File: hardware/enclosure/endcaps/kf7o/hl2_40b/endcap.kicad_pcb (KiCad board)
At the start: 2 copper layers, 106 x 40 mm, 45 parts, among them J2 Male Header, J3 Male Header, J4 Fan, Q1 DTC144E, Q2 IRLML6402, Q3 MULTIFET, Q4 MULTIFET, Q5 MULTIFET, Q6 MULTIFET, Q7 MULTIFET, U1 ACPL-M21L-000E

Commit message: Final IO end plates
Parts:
- added G***: OSHW-logo_silkscreen-back_2mm, HERMESLITE:OSHW-logo_silkscreen-back_2mm, B.Cu at (127.1, 55.1)
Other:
- board text added: "HL2 IO End Plate v1.0 © 2019 SofterHardware"
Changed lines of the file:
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@@
   (general
     (thickness 1.6)
-    (drawings 24)
+    (drawings 25)
     (tracks 281)
     (zones 0)
-    (modules 45)
+    (modules 46)
     (nets 29)
   )
@@
   (title_block
     (title "Hermes-Lite End Plate 40")
-    (date 2019-11-24)
+    (date 2019-12-01)
     (rev 2.0)
     (company SofterHardware)
@@
     )
   )
+  (module HERMESLITE:OSHW-logo_silkscreen-back_2mm (layer B.Cu)
+    (at 127.1 55.1 180)
+    (fp_text reference G*** (at 0 -1.05918 180) (layer B.SilkS) hide
+      (effects (font (size 0.0889 0.0889) (thickness 0.01778)) (justify mirror))
+    )
+    (fp_text value OSHW-logo_silkscreen-back_2mm (at 0 1.05918 180) (layer B.SilkS) hide
+      (effects (font (size 0.0889 0.0889) (thickness 0.01778)) (justify mirror))
+    )
+    (fp_poly (pts (xy 0.60452 -0.89662) (xy 0.59436 -0.89154) (xy 0.5715 -0.8763) (xy 0.53848 -0.85598)
+      (xy 0.49784 -0.82804) (xy 0.45974 -0.80264) (xy 0.42672 -0.77978) (xy 0.40386 -0.76454)
+      (xy 0.3937 -0.75946) (xy 0.38862 -0.762) (xy 0.37084 -0.77216) (xy 0.3429 -0.78486)
+      (xy 0.32766 -0.79248) (xy 0.30226 -0.80518) (xy 0.28956 -0.80772) (xy 0.28702 -0.80264)
+      (xy 0.27686 -0.78486) (xy 0.26416 -0.75184) (xy 0.24384 -0.70866) (xy 0.22352 -0.65786)
+      (xy 0.20066 -0.60198) (xy 0.1778 -0.5461) (xy 0.15494 -0.49276) (xy 0.13462 -0.4445)
+      (xy 0.11938 -0.4064) (xy 0.10922 -0.37846) (xy 0.10414 -0.3683) (xy 0.10668 -0.36576)
+      (xy 0.11938 -0.35306) (xy 0.1397 -0.33782) (xy 0.18796 -0.29718) (xy 0.23368 -0.23876)
+      (xy 0.26416 -0.17272) (xy 0.27178 -0.09906) (xy 0.26416 -0.03302) (xy 0.23876 0.03048)
+      (xy 0.19304 0.09144) (xy 0.13716 0.13462) (xy 0.07112 0.16256) (xy 0 0.17018)
+      (xy -0.06858 0.16256) (xy -0.13462 0.13716) (xy -0.19558 0.09144) (xy -0.21844 0.0635)
+      (xy -0.254 0.00254) (xy -0.27432 -0.05842) (xy -0.27432 -0.07366) (xy -0.27178 -0.14478)
+      (xy -0.25146 -0.21336) (xy -0.2159 -0.27178) (xy -0.16256 -0.32258) (xy -0.15748 -0.32766)
+      (xy -0.13208 -0.34544) (xy -0.11684 -0.3556) (xy -0.10414 -0.36576) (xy -0.19304 -0.58166)
+      (xy -0.20828 -0.61722) (xy -0.23368 -0.67564) (xy -0.254 -0.72644) (xy -0.27178 -0.76708)
+      (xy -0.28448 -0.79248) (xy -0.28956 -0.80518) (xy -0.29718 -0.80518) (xy -0.31242 -0.8001)
+      (xy -0.3429 -0.78486) (xy -0.36322 -0.7747) (xy -0.38608 -0.76454) (xy -0.39624 -0.75946)
+      (xy -0.4064 -0.76454) (xy -0.42672 -0.77978) (xy -0.45974 -0.8001) (xy -0.49784 -0.8255)
+      (xy -0.5334 -0.8509) (xy -0.56896 -0.87376) (xy -0.59182 -0.889) (xy -0.60452 -0.89662)
+      (xy -0.60706 -0.89662) (xy -0.61722 -0.889) (xy -0.63754 -0.87376) (xy -0.66548 -0.84582)
+      (xy -0.70612 -0.80518) (xy -0.71374 -0.8001) (xy -0.74676 -0.76454) (xy -0.7747 -0.73406)
+      (xy -0.79502 -0.71374) (xy -0.8001 -0.70612) (xy -0.79502 -0.69342) (xy -0.77978 -0.66802)
+      (xy -0.75692 -0.635) (xy -0.72898 -0.59436) (xy -0.65786 -0.49022) (xy -0.6985 -0.3937)
+      (xy -0.70866 -0.36322) (xy -0.7239 -0.32766) (xy -0.7366 -0.30226) (xy -0.74168 -0.28956)
+      (xy -0.75184 -0.28702) (xy -0.77978 -0.2794) (xy -0.81788 -0.27178) (xy -0.8636 -0.26416)
+      (xy -0.90932 -0.254) (xy -0.94742 -0.24638) (xy -0.9779 -0.2413) (xy -0.9906 -0.23876)
+      (xy -0.99314 -0.23622) (xy -0.99568 -0.23114) (xy -0.99822 -0.21844) (xy -0.99822 -0.19304)
+      (xy -0.99822 -0.15494) (xy -0.99822 -0.09906) (xy -0.99822 -0.09398) (xy -0.99822 -0.04064)
+      (xy -0.99822 0) (xy -0.99568 0.0254) (xy -0.99314 0.03556) (xy -0.98044 0.04064)
+      (xy -0.9525 0.04572) (xy -0.9144 0.05334) (xy -0.86614 0.0635) (xy -0.8636 0.0635)
+      (xy -0.81534 0.07112) (xy -0.77724 0.08128) (xy -0.7493 0.08636) (xy -0.7366 0.09144)
+      (xy -0.73406 0.09398) (xy -0.7239 0.11176) (xy -0.7112 0.14224) (xy -0.69596 0.1778)
+      (xy -0.68072 0.21336) (xy -0.66548 0.24892) (xy -0.65786 0.27178) (xy -0.65532 0.28448)
+      (xy -0.66294 0.29464) (xy -0.67818 0.32004) (xy -0.70104 0.35306) (xy -0.72898 0.3937)
+      (xy -0.73152 0.39878) (xy -0.75946 0.43688) (xy -0.77978 0.47244) (xy -0.79502 0.4953)
+      (xy -0.8001 0.50546) (xy -0.8001 0.508) (xy -0.79248 0.51816) (xy -0.77216 0.54102)
+      (xy -0.74168 0.5715) (xy -0.70612 0.60706) (xy -0.69596 0.61722) (xy -0.65786 0.65532)
+      (xy -0.62992 0.68072) (xy -0.61214 0.69342) (xy -0.60452 0.6985) (xy -0.60452 0.69596)
+      (xy -0.59182 0.69088) (xy -0.56642 0.6731) (xy -0.5334 0.65024) (xy -0.49276 0.6223)
+      (xy -0.49022 0.61976) (xy -0.44958 0.59436) (xy -0.41656 0.5715) (xy -0.3937 0.55626)
+      (xy -0.38354 0.54864) (xy -0.381 0.54864) (xy -0.36576 0.55372) (xy -0.33528 0.56388)
+      (xy -0.30226 0.57658) (xy -0.26416 0.59182) (xy -0.23114 0.60706) (xy -0.20574 0.61722)
+      (xy -0.19304 0.62484) (xy -0.18796 0.64008) (xy -0.18288 0.67056) (xy -0.17272 0.7112)
+      (xy -0.1651 0.75946) (xy -0.16256 0.76708) (xy -0.15494 0.81534) (xy -0.14732 0.85344)
+      (xy -0.1397 0.88138) (xy -0.13716 0.89408) (xy -0.13208 0.89408) (xy -0.10668 0.89662)
+      (xy -0.07112 0.89662) (xy -0.02794 0.89662) (xy 0.01524 0.89662) (xy 0.05842 0.89662)
+      (xy 0.09652 0.89408) (xy 0.12192 0.89408) (xy 0.13462 0.89154) (xy 0.13462 0.889)
+      (xy 0.1397 0.8763) (xy 0.14478 0.84582) (xy 0.15494 0.80518) (xy 0.16256 0.75438)
+      (xy 0.1651 0.74676) (xy 0.17272 0.6985) (xy 0.18288 0.6604) (xy 0.18796 0.63246)
+      (xy 0.1905 0.6223) (xy 0.19558 0.61976) (xy 0.21336 0.61214) (xy 0.24638 0.59944)
+      (xy 0.28702 0.58166) (xy 0.37846 0.5461) (xy 0.49022 0.6223) (xy 0.50038 0.62992)
+      (xy 0.54102 0.65786) (xy 0.57404 0.67818) (xy 0.5969 0.69342) (xy 0.60706 0.6985)
+      (xy 0.61722 0.68834) (xy 0.64008 0.66802) (xy 0.67056 0.63754) (xy 0.70612 0.60452)
+      (xy 0.73152 0.57658) (xy 0.762 0.5461) (xy 0.78232 0.52578) (xy 0.79248 0.51054)
+      (xy 0.79756 0.50292) (xy 0.79502 0.49784) (xy 0.78994 0.48514) (xy 0.77216 0.46228)
+      (xy 0.7493 0.42672) (xy 0.72136 0.38862) (xy 0.6985 0.35306) (xy 0.67564 0.3175)
+      (xy 0.6604 0.28956) (xy 0.65278 0.27686) (xy 0.65532 0.27178) (xy 0.66294 0.24892)
+      (xy 0.67564 0.2159) (xy 0.69342 0.17526) (xy 0.73152 0.08636) (xy 0.78994 0.0762)
+      (xy 0.8255 0.06858) (xy 0.8763 0.06096) (xy 0.92202 0.0508) (xy 0.99568 0.03556)
+      (xy 0.99822 -0.23114) (xy 0.98806 -0.23622) (xy 0.97536 -0.2413) (xy 0.94996 -0.24638)
+      (xy 0.90932 -0.254) (xy 0.8636 -0.26162) (xy 0.8255 -0.26924) (xy 0.78486 -0.27686)
+      (xy 0.75692 -0.28194) (xy 0.74422 -0.28448) (xy 0.74168 -0.28956) (xy 0.73152 -0.30988)
+      (xy 0.71628 -0.34036) (xy 0.70104 -0.37592) (xy 0.6858 -0.41402) (xy 0.6731 -0.44958)
+      (xy 0.66294 -0.47498) (xy 0.65786 -0.49022) (xy 0.66294 -0.50038) (xy 0.67818 -0.52324)
+      (xy 0.70104 -0.55626) (xy 0.72644 -0.59436) (xy 0.75438 -0.635) (xy 0.77724 -0.66802)
+      (xy 0.79248 -0.69342) (xy 0.8001 -0.70358) (xy 0.79502 -0.7112) (xy 0.77978 -0.72898)
+      (xy 0.75184 -0.75946) (xy 0.70612 -0.80518) (xy 0.6985 -0.81026) (xy 0.66548 -0.84582)
+      (xy 0.635 -0.87122) (xy 0.61468 -0.89154) (xy 0.60452 -0.89662)) (layer B.SilkS) (width 0.00254))
+  )
+  (gr_text "HL2 IO End Plate v1.0\n© 2019 SofterHardware" (at 147.3 55.3) (layer B.SilkS)
+    (effects (font (size 1 1) (thickness 0.12)) (justify left mirror))
+  )
   (gr_text Hermes-Lite (at 54 69.8 270) (layer Eco1.User)

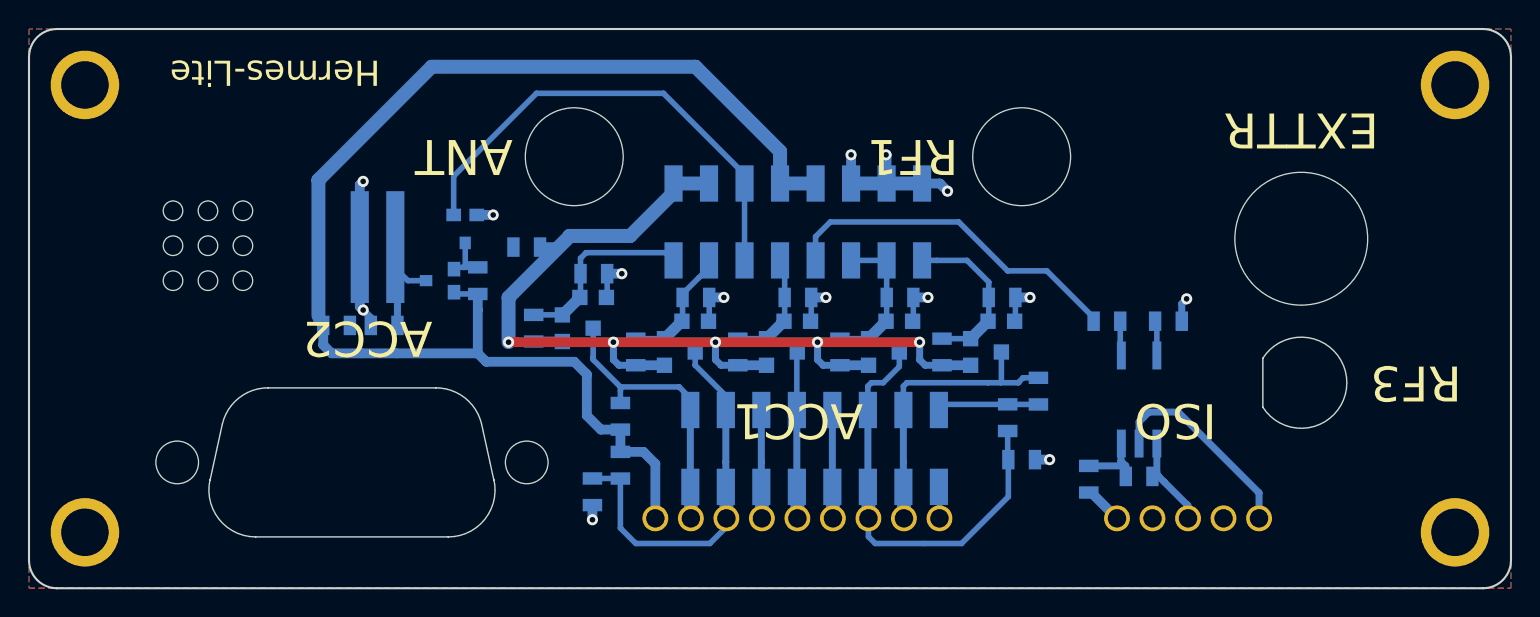
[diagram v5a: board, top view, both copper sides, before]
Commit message: Add LPF for fan on latest end plates
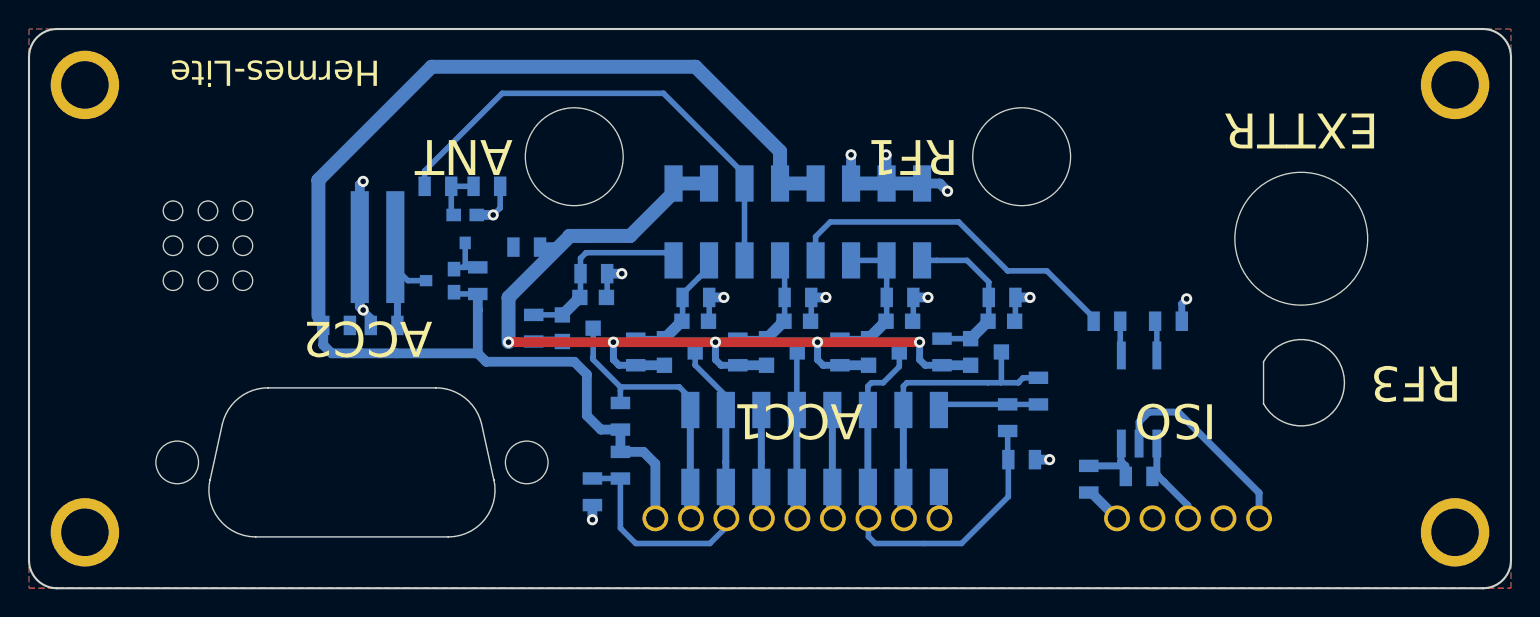
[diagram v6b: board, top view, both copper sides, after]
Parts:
- added C5: 0.1uF, endcaplib:SMD-0805, B.Cu at (82.8, 61.2)
- added R18: 1K, endcaplib:SMD-0805, B.Cu at (79.2, 61.2)
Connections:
- Q1 pad 1: Net-(J2-Pad5) -> Net-(C5-Pad2)
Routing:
- net Net-(C5-Pad2): track 0.00 -> 3.72 mm
- net GNDS: track 43.1 -> 45.4 mm
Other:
- board text added: "HL2 IO End Plate v2.1 © 2020 SofterHardware"
- board text removed: "HL2 IO End Plate v1.0 © 2019 SofterHardware"
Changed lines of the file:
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@@
-(kicad_pcb (version 20171130) (host pcbnew 5.0.2-bee76a0~70~ubuntu16.04.1)
+(kicad_pcb (version 20171130) (host pcbnew 5.1.5-52549c5~84~ubuntu18.04.1)
   (general
     (thickness 1.6)
     (drawings 25)
-    (tracks 281)
+    (tracks 286)
     (zones 0)
-    (modules 46)
-    (nets 29)
+    (modules 48)
+    (nets 30)
   )
   (page USLetter)
@@
     (title "Hermes-Lite End Plate 40")
     (date 2019-12-01)
-    (rev 2.0)
+    (rev 2.1)
     (company SofterHardware)
     (comment 1 "KF7O Steve Haynal")
@@
     (zone_45_only no)
     (trace_min 0.2)
-    (segment_width 0.2)
-    (edge_width 0.15)
     (via_size 0.8)
     (via_drill 0.4)
@@
     (uvia_min_size 0.2)
     (uvia_min_drill 0.1)
+    (edge_width 0.15)
+    (segment_width 0.2)
     (pcb_text_width 0.3)
     (pcb_text_size 1.5 1.5)
@@
   (net 27 "Net-(C4-Pad2)")
   (net 28 "Net-(J3-Pad15)")
+  (net 29 "Net-(C5-Pad2)")
   (net_class Default "This is the default net class."
     (clearance 0.2)
@@
     (add_net "Net-(C1-Pad2)")
     (add_net "Net-(C4-Pad2)")
+    (add_net "Net-(C5-Pad2)")
     (add_net "Net-(FB1-Pad1)")
     (add_net "Net-(ISO1-Pad2)")
@@
     (add_net VSUP)
     (add_net Vlvds)
+  )
+  (module endcaplib:sma_panel (layer B.Cu)
+    (at 141 75.3)
+    (fp_text reference RF3 (at 0 5.5) (layer B.SilkS)
+      (effects (font (size 0.8 0.8) (thickness 0.1)) (justify mirror))
+    )
+    (fp_text value SMA (at 0 -4.25) (layer B.Fab)
+      (effects (font (size 1 1) (thickness 0.15)) (justify mirror))
+    )
+    (fp_arc (start 0 0) (end -2.699999 -1.499999) (angle 302.1346022) (layer Edge.Cuts) (width 0.1))
+    (fp_line (start -2.7 1.5) (end -2.7 -1.5) (layer Edge.Cuts) (width 0.1))
+  )
+  (module endcaplib:SMD-0805 (layer B.Cu)
+    (at 82.75 61.25 180)
+    (attr smd)
+    (fp_text reference C5 (at -2.25 -1.4) (layer B.SilkS)
+      (effects (font (size 0.8 0.8) (thickness 0.1)) (justify mirror))
+    )
+    (fp_text value 0.1uF (at 0 -0.381) (layer B.SilkS) hide
+      (effects (font (size 0.8 0.8) (thickness 0.1)) (justify mirror))
+    )
+    (fp_line (start 1.524 -0.762) (end 0.508 -0.762) (layer B.SilkS) (width 0.1))
+    (fp_line (start 1.524 0.762) (end 1.524 -0.762) (layer B.SilkS) (width 0.1))
+    (fp_line (start 0.508 0.762) (end 1.524 0.762) (layer B.SilkS) (width 0.1))
+    (fp_line (start -1.524 0.762) (end -0.508 0.762) (layer B.SilkS) (width 0.1))
+    (fp_line (start -1.524 -0.762) (end -1.524 0.762) (layer B.SilkS) (width 0.1))
+    (fp_line (start -0.508 -0.762) (end -1.524 -0.762) (layer B.SilkS) (width 0.1))
+    (pad 2 smd rect (at 0.9525 0 180) (size 0.889 1.397) (layers B.Cu B.Paste B.Mask)
+      (net 29 "Net-(C5-Pad2)"))
+    (pad 1 smd rect (at -0.9525 0 180) (size 0.889 1.397) (layers B.Cu B.Paste B.Mask)
+      (net 2 GNDS))
+    (model smd/chip_cms.wrl
+      (at (xyz 0 0 0))
+      (scale (xyz 0.1 0.1 0.1))
+      (rotate (xyz 0 0 0))
+    )
+  )
+  (module endcaplib:SMD-0805 (layer B.Cu)
+    (at 79.25 61.25)
+    (attr smd)
+    (fp_text reference R18 (at -0.75 1.5) (layer B.SilkS)
+      (effects (font (size 0.8 0.8) (thickness 0.1)) (justify mirror))
+    )
+    (fp_text value 1K (at 0 -0.381) (layer B.SilkS) hide
+      (effects (font (size 0.8 0.8) (thickness 0.1)) (justify mirror))
+    )
+    (fp_line (start -0.508 -0.762) (end -1.524 -0.762) (layer B.SilkS) (width 0.1))
+    (fp_line (start -1.524 -0.762) (end -1.524 0.762) (layer B.SilkS) (width 0.1))
+    (fp_line (start -1.524 0.762) (end -0.508 0.762) (layer B.SilkS) (width 0.1))
+    (fp_line (start 0.508 0.762) (end 1.524 0.762) (layer B.SilkS) (width 0.1))
+    (fp_line (start 1.524 0.762) (end 1.524 -0.762) (layer B.SilkS) (width 0.1))
+    (fp_line (start 1.524 -0.762) (end 0.508 -0.762) (layer B.SilkS) (width 0.1))
+    (pad 1 smd rect (at -0.9525 0) (size 0.889 1.397) (layers B.Cu B.Paste B.Mask)
+      (net 6 "Net-(J2-Pad5)"))
+    (pad 2 smd rect (at 0.9525 0) (size 0.889 1.397) (layers B.Cu B.Paste B.Mask)
+      (net 29 "Net-(C5-Pad2)"))
+    (model smd/chip_cms.wrl
+      (at (xyz 0 0 0))
+      (scale (xyz 0.1 0.1 0.1))
+      (rotate (xyz 0 0 0))
+    )
   )
   (module endcaplib:SMD-0805 (layer B.Cu)
@@
   (module endcaplib:SOT23_3 (layer B.Cu)
     (at 81.2 63.3)
-    (fp_text reference Q1 (at -2.7 0) (layer B.SilkS)
+    (fp_text reference Q1 (at -2.7 1.45) (layer B.SilkS)
       (effects (font (size 0.8 0.8) (thickness 0.1)) (justify mirror))
     )
@@
       (net 1 "Net-(Q1-Pad3)"))
     (pad 1 smd rect (at -0.825 0) (size 1.05 0.9) (layers B.Cu B.Paste B.Mask)
-      (net 6 "Net-(J2-Pad5)"))
+      (net 29 "Net-(C5-Pad2)"))
   )
   (module endcaplib:SOT23_3 (layer B.Cu)
@@
       (rotate (xyz 0 0 0))
     )
-  )
-  (module endcaplib:sma_panel (layer B.Cu)
-    (at 141 75.3)
-    (fp_text reference RF3 (at 0 5.5) (layer B.SilkS)
-      (effects (font (size 0.8 0.8) (thickness 0.1)) (justify mirror))
-    )
-    (fp_text value SMA (at 0 -4.25) (layer B.Fab)
-      (effects (font (size 1 1) (thickness 0.15)) (justify mirror))
-    )
-    (fp_line (start -2.75 1.75) (end -2.75 -1.75) (layer Edge.Cuts) (width 0.1))
-    (fp_arc (start 0 0) (end -2.749999 -1.749999) (angle 295.0576154) (layer Edge.Cuts) (width 0.1))
   )
   (module endcaplib:male_header_2 (layer B.Cu)
@@
       (xy 0.635 -0.87122) (xy 0.61468 -0.89154) (xy 0.60452 -0.89662)) (layer B.SilkS) (width 0.00254))
   )
-  (gr_text "HL2 IO End Plate v1.0\n© 2019 SofterHardware" (at 147.3 55.3) (layer B.SilkS)
+  (gr_text "HL2 IO End Plate v2.1\n© 2020 SofterHardware" (at 147.3 55.3) (layer B.SilkS)
     (effects (font (size 1 1) (thickness 0.12)) (justify left mirror))
   )
@@
   (via (at 90.3 85.1) (size 0.8) (drill 0.4) (layers F.Cu B.Cu) (net 2))
   (segment (start 90.3 84.0525) (end 90.3 85.1) (width 0.7) (layer B.Cu) (net 2))
+  (segment (start 83.7025 62.7975) (end 83.2 63.3) (width 0.4) (layer B.Cu) (net 2))
+  (segment (start 83.7025 61.25) (end 83.7025 62.7975) (width 0.4) (layer B.Cu) (net 2))
   (segment (start 115.3025 74.05) (end 115.3 74.0525) (width 0.7) (layer B.Cu) (net 3))
   (segment (start 117.35 74.05) (end 115.3025 74.05) (width 0.7) (layer B.Cu) (net 3))
@@
   (segment (start 98.64 67.06) (end 97.9 67.8) (width 0.4) (layer B.Cu) (net 5))
   (segment (start 101.18 66.55) (end 101.18 61.05) (width 0.4) (layer B.Cu) (net 6))
-  (segment (start 80.375 60.525) (end 80.375 63.3) (width 0.4) (layer B.Cu) (net 6))
+  (segment (start 78.2975 60.1515) (end 78.2975 61.25) (width 0.4) (layer B.Cu) (net 6))
+  (segment (start 83.849 54.6) (end 78.2975 60.1515) (width 0.4) (layer B.Cu) (net 6))
+  (segment (start 95.38 54.6) (end 83.849 54.6) (width 0.4) (layer B.Cu) (net 6))
+  (segment (start 101.18 60.4) (end 95.38 54.6) (width 0.4) (layer B.Cu) (net 6))
   (segment (start 101.18 61.05) (end 101.18 60.4) (width 0.4) (layer B.Cu) (net 6))
-  (segment (start 101.18 60.4) (end 95.38 54.6) (width 0.4) (layer B.Cu) (net 6))
-  (segment (start 95.38 54.6) (end 86.3 54.6) (width 0.4) (layer B.Cu) (net 6))
-  (segment (start 86.3 54.6) (end 80.375 60.525) (width 0.4) (layer B.Cu) (net 6))
   (segment (start 102.7475 72.1475) (end 102.75 72.15) (width 0.25) (layer B.Cu) (net 7))
   (segment (start 100.7 72.1475) (end 102.7475 72.1475) (width 0.25) (layer B.Cu) (net 7))
@@
   (segment (start 115.4825 76.8475) (end 115.08 77.25) (width 0.4) (layer B.Cu) (net 28))
   (segment (start 120 76.8475) (end 115.4825 76.8475) (width 0.4) (layer B.Cu) (net 28))
+  (segment (start 80.2025 61.25) (end 81.7975 61.25) (width 0.4) (layer B.Cu) (net 29))
+  (segment (start 80.2025 63.1275) (end 80.375 63.3) (width 0.4) (layer B.Cu) (net 29))
+  (segment (start 80.2025 61.25) (end 80.2025 63.1275) (width 0.4) (layer B.Cu) (net 29))
   (zone (net 2) (net_name GNDS) (layer F.Cu) (hatch edge 0.508)
     (connect_pads (clearance 0.3))
